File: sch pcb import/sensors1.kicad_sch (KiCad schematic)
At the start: 41 parts, among them Q401 SS8050, U401 BMP280, U402 BMP280, U403 BME280, U404 HMC5883L-TR, U405 MPU-6050, U406 MMC5983MA, U407 DS3231M, U408 LSM6DSL

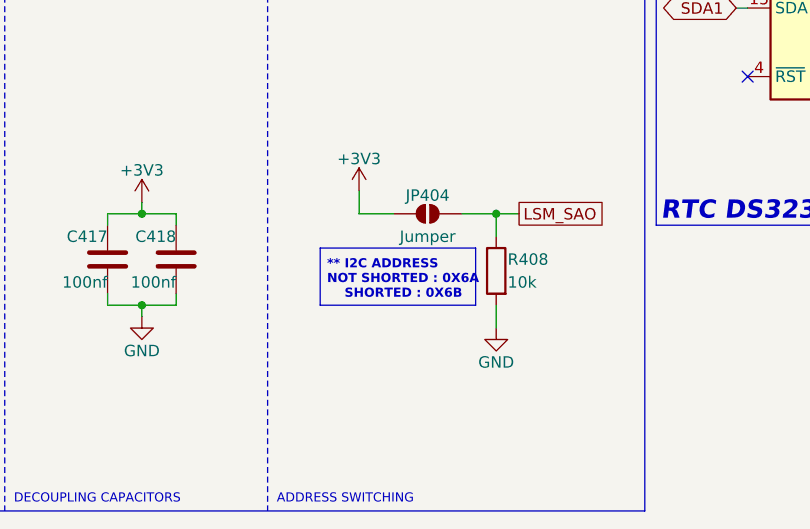
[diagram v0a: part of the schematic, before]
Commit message: added servo and finished esp32 connections
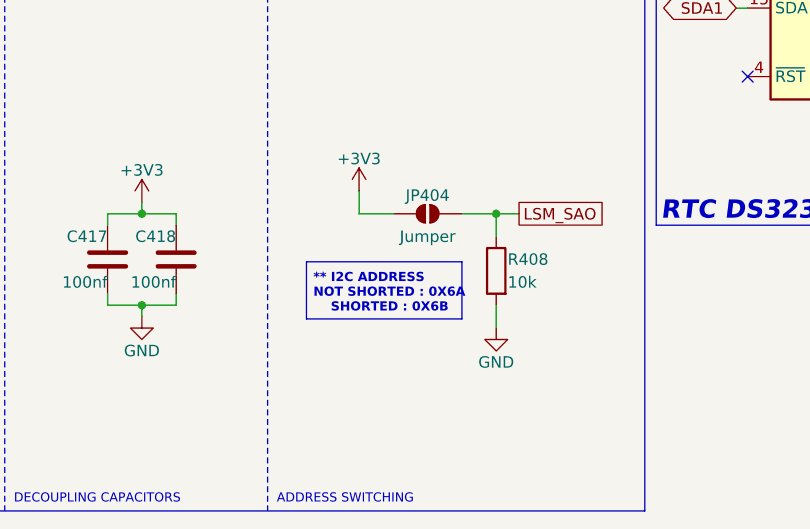
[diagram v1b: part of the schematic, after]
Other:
- company: Done by :- Arudhran -> Drawn by :- Arudhran
- title: AVIONICS PCB -> VECTRON
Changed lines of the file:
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@@
 	(paper "A4")
 	(title_block
-		(title "AVIONICS PCB")
-		(date "2025-05-27")
+		(title "VECTRON")
+		(date "2025-06-10")
 		(rev "1.0.0")
-		(company "Done by :- Arudhran")
+		(company "Drawn by :- Arudhran")
 	)
 	(rectangle
@@
 	)
 	(rectangle
-		(start 112.522 167.64)
-		(end 129.794 173.99)
+		(start 110.998 169.164)
+		(end 128.27 175.514)
 		(stroke
 			(width 0)
@@
 	(text "** I2C ADDRESS\nNOT SHORTED : 0X6A\n    SHORTED : 0X6B"
 		(exclude_from_sim no)
-		(at 113.284 171.196 0)
-		(effects
-			(font
+		(at 111.76 172.72 0)
+		(effects
+			(font

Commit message: minor changes
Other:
- title: VECTRON -> VECTRON-V1
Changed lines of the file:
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@@
 	(paper "A4")
 	(title_block
-		(title "VECTRON")
-		(date "2025-06-10")
+		(title "VECTRON-V1")
+		(date "2025-06-13")
 		(rev "1.0.0")
 		(company "Drawn by :- Arudhran")

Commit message: minor changes
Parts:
- C401, C402, C403, C404, C405, C406, C407, C408, C409, C410, C411, C412, C413, C414, C415, C416, C417, C418: footprint (none) -> Capacitor_SMD:C_0603_1608Metric
- D401: footprint (none) -> LED_SMD:LED_0603_1608Metric
- JP401, JP402, JP403, JP404: footprint (none) -> Jumper:SolderJumper-2_P1.3mm_Open_RoundedPad1.0x1.5mm
- R401, R402, R403, R404, R405, R406, R407, R408: footprint (none) -> Resistor_SMD:R_0603_1608Metric
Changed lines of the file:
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@@
 			)
 		)
-		(property "Footprint" ""
+		(property "Footprint" "Capacitor_SMD:C_0603_1608Metric"
 			(at 206.7052 152.4 0)
 			(effects
@@
 			)
 		)
-		(property "Footprint" ""
+		(property "Footprint" "Resistor_SMD:R_0603_1608Metric"
 			(at 89.408 29.21 90)
 			(effects
@@
 			)
 		)
-		(property "Footprint" ""
+		(property "Footprint" "Capacitor_SMD:C_0603_1608Metric"
 			(at 266.3952 43.18 0)
 			(effects
@@
 			)
 		)
-		(property "Footprint" ""
+		(property "Footprint" "Capacitor_SMD:C_0603_1608Metric"
 			(at 56.8452 36.83 0)
 			(effects
@@
 			)
 		)
-		(property "Footprint" ""
+		(property "Footprint" "Resistor_SMD:R_0603_1608Metric"
 			(at 165.1 98.298 90)
 			(effects
@@
 			)
 		)
-		(property "Footprint" ""
+		(property "Footprint" "Capacitor_SMD:C_0603_1608Metric"
 			(at 72.0852 124.46 0)
 			(effects
@@
 			)
 		)
-		(property "Footprint" ""
+		(property "Footprint" "Capacitor_SMD:C_0603_1608Metric"
 			(at 267.6652 134.62 0)
 			(effects
@@
 			)
 		)
-		(property "Footprint" ""
+		(property "Footprint" "Jumper:SolderJumper-2_P1.3mm_Open_RoundedPad1.0x1.5mm"
 			(at 124.46 163.83 0)
 			(effects
@@
 			)
 		)
-		(property "Footprint" ""
+		(property "Footprint" "Capacitor_SMD:C_0603_1608Metric"
 			(at 64.4652 36.83 0)
 			(effects
@@
 			)
 		)
-		(property "Footprint" ""
+		(property "Footprint" "Resistor_SMD:R_0603_1608Metric"
 			(at 127.508 30.48 90)
 			(effects
@@
 			)
 		)
-		(property "Footprint" ""
+		(property "Footprint" "Capacitor_SMD:C_0603_1608Metric"
 			(at 214.3252 105.41 0)
 			(effects
@@
 			)
 		)
-		(property "Footprint" ""
+		(property "Footprint" "Capacitor_SMD:C_0603_1608Metric"
 			(at 279.0952 82.55 0)
 			(effects
@@
 			)
 		)
-		(property "Footprint" ""
+		(property "Footprint" "Capacitor_SMD:C_0603_1608Metric"
 			(at 101.2952 114.3 0)
 			(effects
@@
 			)
 		)
-		(property "Footprint" ""
+		(property "Footprint" "Resistor_SMD:R_0603_1608Metric"
 			(at 132.588 114.3 90)
 			(effects
@@
 			)
 		)
-		(property "Footprint" ""
+		(property "Footprint" "Capacitor_SMD:C_0603_1608Metric"
 			(at 97.4852 172.72 0)
 			(effects
@@
 			)
 		)
-		(property "Footprint" ""
+		(property "Footprint" "Resistor_SMD:R_0603_1608Metric"
 			(at 44.45 151.638 90)
 			(effects
@@
 			)
 		)
-		(property "Footprint" ""
+		(property "Footprint" "Capacitor_SMD:C_0603_1608Metric"
 			(at 271.4752 82.55 0)
 			(effects
@@
 			)
 		)
-		(property "Footprint" ""
+		(property "Footprint" "Capacitor_SMD:C_0603_1608Metric"
 			(at 163.83 128.5748 0)
 			(effects
@@
 			)
 		)
-		(property "Footprint" ""
+		(property "Footprint" "Resistor_SMD:R_0603_1608Metric"
 			(at 133.858 170.18 90)
 			(effects
@@
 			)
 		)
-		(property "Footprint" ""
+		(property "Footprint" "Jumper:SolderJumper-2_P1.3mm_Open_RoundedPad1.0x1.5mm"
 			(at 118.11 24.13 0)
 			(effects
@@
 			)
 		)
-		(property "Footprint" ""
+		(property "Footprint" "Capacitor_SMD:C_0603_1608Metric"
 			(at 89.8652 172.72 0)
 			(effects
@@
 			)
 		)
-		(property "Footprint" ""
+		(property "Footprint" "LED_SMD:LED_0603_1608Metric"
 			(at 168.91 83.82 0)
 			(effects
@@
 			)
 		)
-		(property "Footprint" ""
+		(property "Footprint" "Jumper:SolderJumper-2_P1.3mm_Open_RoundedPad1.0x1.5mm"
 			(at 81.28 22.86 0)
 			(effects
@@
 			)
 		)
-		(property "Footprint" ""
+		(property "Footprint" "Capacitor_SMD:C_0603_1608Metric"
 			(at 93.6752 114.3 0)
 			(effects
@@
 			)
 		)
-		(property "Footprint" ""
+		(property "Footprint" "Capacitor_SMD:C_0603_1608Metric"
 			(at 79.7052 124.46 0)
 			(effects
@@
 			)
 		)
-		(property "Footprint" ""
+		(property "Footprint" "Capacitor_SMD:C_0603_1608Metric"
 			(at 279.0952 107.95 0)
 			(effects
@@
 			)
 		)
-		(property "Footprint" ""
+		(property "Footprint" "Resistor_SMD:R_0603_1608Metric"
 			(at 30.48 24.638 90)
 			(effects
@@
 			)
 		)
-		(property "Footprint" ""
+		(property "Footprint" "Jumper:SolderJumper-2_P1.3mm_Open_RoundedPad1.0x1.5mm"
 			(at 123.19 107.95 0)
 			(effects
@@
 			)
 		)
-		(property "Footprint" ""
+		(property "Footprint" "Capacitor_SMD:C_0603_1608Metric"
 			(at 274.0152 43.18 0)
 			(effects
@@
 			)
 		)
-		(property "Footprint" ""
+		(property "Footprint" "Capacitor_SMD:C_0603_1608Metric"
 			(at 275.2852 134.62 0)
 			(effects
@@
 			)
 		)
-		(property "Footprint" ""
+		(property "Footprint" "Resistor_SMD:R_0603_1608Metric"
 			(at 218.44 25.908 90)
 			(effects

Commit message: minor changes
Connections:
- net BUZZER_NEGATIVE: now also Q401.3 (C); no longer Q401.2 (E)
- net GND: now also Q401.2 (E); no longer Q401.3 (C)
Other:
- company: Drawn by :- Arudhran -> (none)
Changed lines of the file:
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@@
 		(date "2025-06-13")
 		(rev "1.0.0")
-		(company "Drawn by :- Arudhran")
+		(comment 9 "ARUDHRAN")
 	)
 	(rectangle
@@
 	(text "MMC5983MA (REDUNDANT)"
 		(exclude_from_sim no)
-		(at 196.85 163.576 0)
+		(at 196.85 162.56 0)
 		(effects
 			(font
@@
 		(lib_id "Transistor_BJT:SS8050")
 		(at 175.26 96.52 0)
-		(mirror x)
 		(unit 1)
 		(exclude_from_sim no)
@@
 		(dnp no)
 		(property "Reference" "Q401"
-			(at 179.705 94.615 0)
+			(at 179.705 98.425 0)
 			(effects
 				(font
@@
 		)
 		(property "Value" "SS8050"
-			(at 179.705 97.155 0)
+			(at 179.705 95.885 0)
 			(effects
 				(font
@@
 		)
 		(property "Footprint" "Package_TO_SOT_SMD:SOT-23-3"
-			(at 180.34 89.154 0)
+			(at 180.34 103.886 0)
 			(effects
 				(font
@@
 		)
 		(property "Datasheet" "http://www.secosgmbh.com/datasheet/products/SSMPTransistor/SOT-23/SS8050.pdf"
-			(at 180.34 91.694 0)
+			(at 180.34 101.346 0)
 			(effects
 				(font
@@
 		)
 		(property "Description" "General Purpose NPN Transistor, 1.5A Ic, 25V Vce, SOT-23"
-			(at 209.296 94.234 0)
+			(at 209.296 98.806 0)
 			(effects
 				(font
